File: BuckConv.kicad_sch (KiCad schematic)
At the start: 8 parts, among them U2 TPS5430DDA

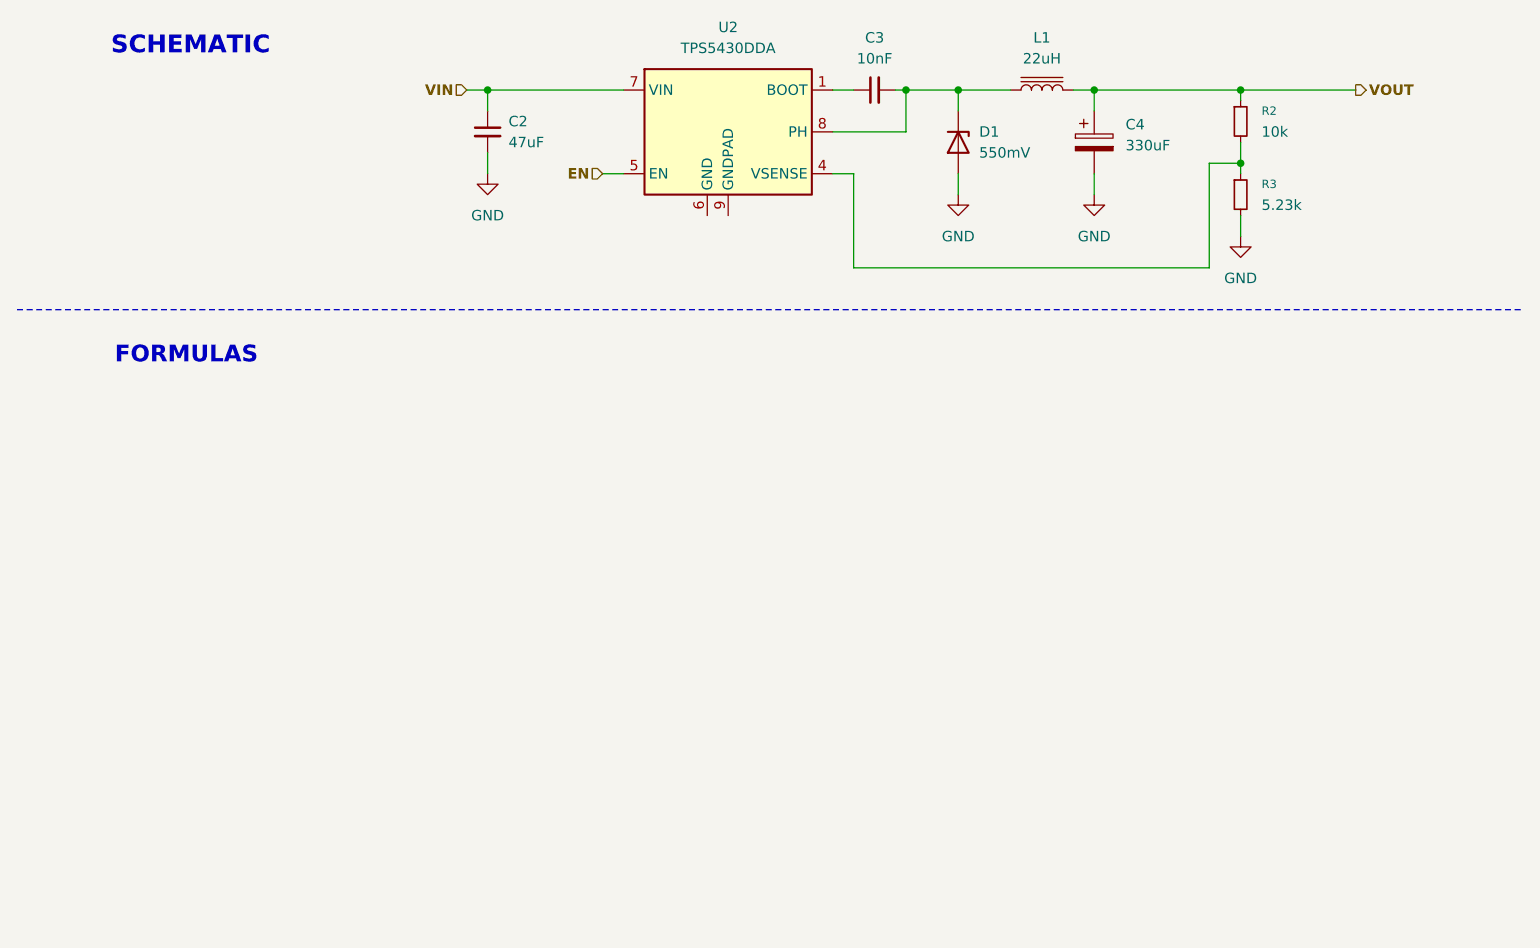
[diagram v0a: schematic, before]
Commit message: Actualizacion de esquematicos de fuente tipo Buck
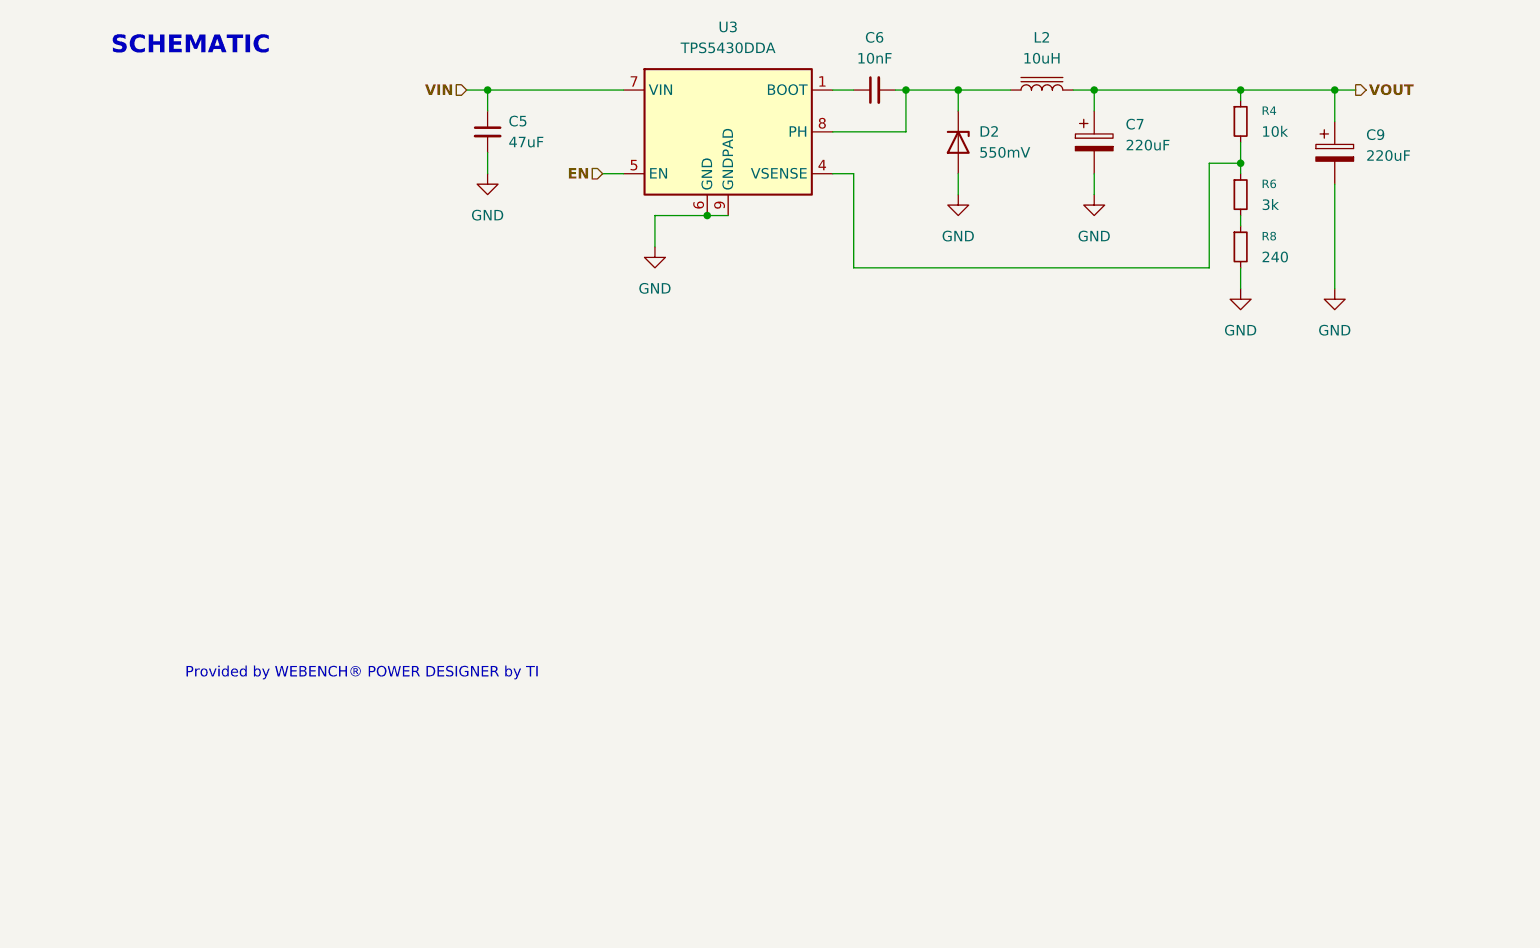
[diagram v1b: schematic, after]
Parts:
- removed R3: 5.23k, symbol Device:R_Small
- added C9: 220uF, symbol Device:C_Polarized
- added R6: 3k, symbol Device:R_Small
- added R8: 240, symbol Device:R_Small
- C7: renamed from C4; value 330uF -> 220uF
- L2: renamed from L1; value 22uH -> 10uH
- renumbered C2 to C5, C3 to C6, D1 to D2, R2 to R4, U2 to U3
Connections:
- net GND: now also U3.6 (GND), U3.9 (GNDPAD), C9.2, R8.2
- net VOUT: now also C9.1
- net at R4.2, U3.4 (VSENSE): now also R6.1
- new net: R6.2, R8.1
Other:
- note added: "Provided by WEBENCH® POWER DESIGNER by TI"
- note removed: "FORMULAS"

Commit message: Semi finished the regulator-section
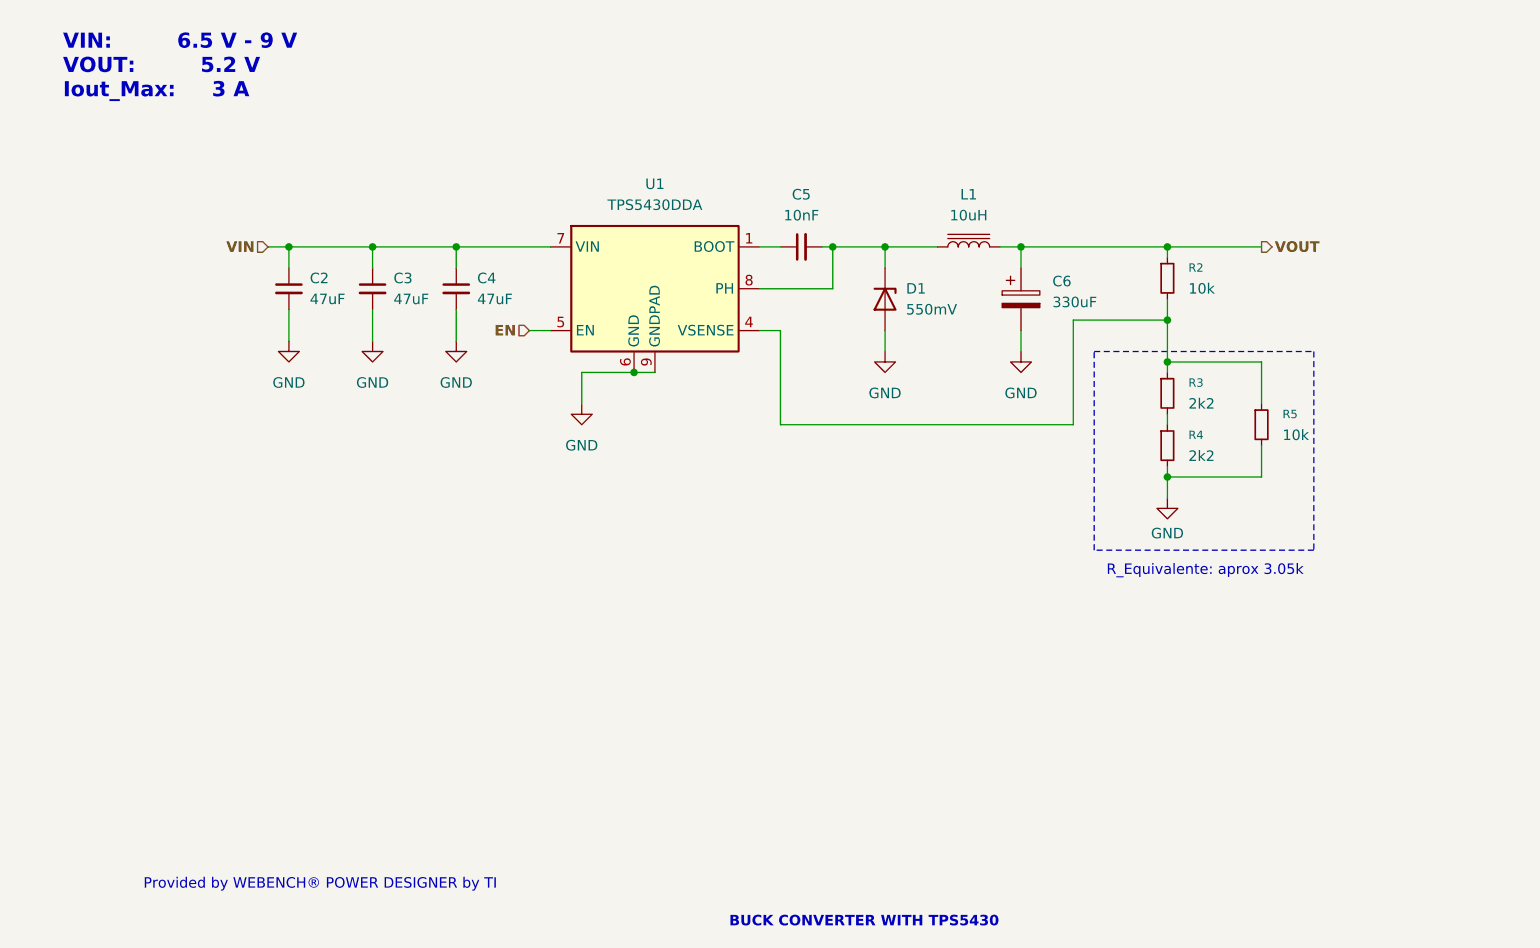
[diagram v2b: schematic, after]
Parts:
- removed C9: 220uF, symbol Device:C_Polarized
- removed R8: 240, symbol Device:R_Small
- added C3, C4: 47uF, Capacitor_SMD:C_0805_2012Metric, symbol Device:C_Small
- added R4: 2k2, Resistor_SMD:R_0805_2012Metric, symbol Device:R_Small
- added R5: 10k, Resistor_SMD:R_0805_2012Metric, symbol Device:R_Small
- C2: renamed from C5; footprint (none) -> Capacitor_SMD:C_0805_2012Metric
- C5: renamed from C6; footprint (none) -> Capacitor_SMD:C_0805_2012Metric
- C6: renamed from C7; value 220uF -> 330uF; footprint (none) -> Capacitor_SMD:C_0805_2012Metric
- D1: renamed from D2; footprint (none) -> Capacitor_SMD:C_0805_2012Metric
- L1: renamed from L2; footprint (none) -> Inductor_SMD:L_Sumida_CDMC6D28_7.25x6.5mm
- R2: renamed from R4; footprint (none) -> Resistor_SMD:R_0805_2012Metric
- R3: renamed from R6; value 3k -> 2k2; footprint (none) -> Resistor_SMD:R_0805_2012Metric
- renumbered U3 to U1
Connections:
- net GND: now also C3.2, C4.2, R4.2, R5.2
- net VIN: now also C3.1, C4.1
- net at R2.2, R3.1, U1.4 (VSENSE): now also R5.1
- net at R3.2: now also R4.1
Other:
- note added: "BUCK CONVERTER WITH TPS5430"
- note added: "R_Equivalente: aprox 3.05k"
- note added: "VIN: 6.5 V - 9 V VOUT: 5.2 V Iout_Max: 3 A"
- note removed: "SCHEMATIC"
- moved on the sheet: C2, C5, C6, D1, L1, R2, R3, U1
